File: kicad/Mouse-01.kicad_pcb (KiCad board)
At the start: 2 copper layers, 54 x 62 mm, 92 parts, among them P1 MT-ENC, P2 MT-ENC, P3 Battery_A, P4 Battery_B, P5 SWD, P6 UART, Q1 IRLML6402, Q2 IRFML8244, Q3 IRFML8244, Q4 BSS138, SW1 RESET, SW2 Power, SW3 BUTTON, U1 STM32F405RGTx, U2 DRV8835, U3 DRV8835, U4 LXDC55FAAA-203, U5 REF1933, U6 LT1963ES8, U7 AD8604, U8 MPU6500

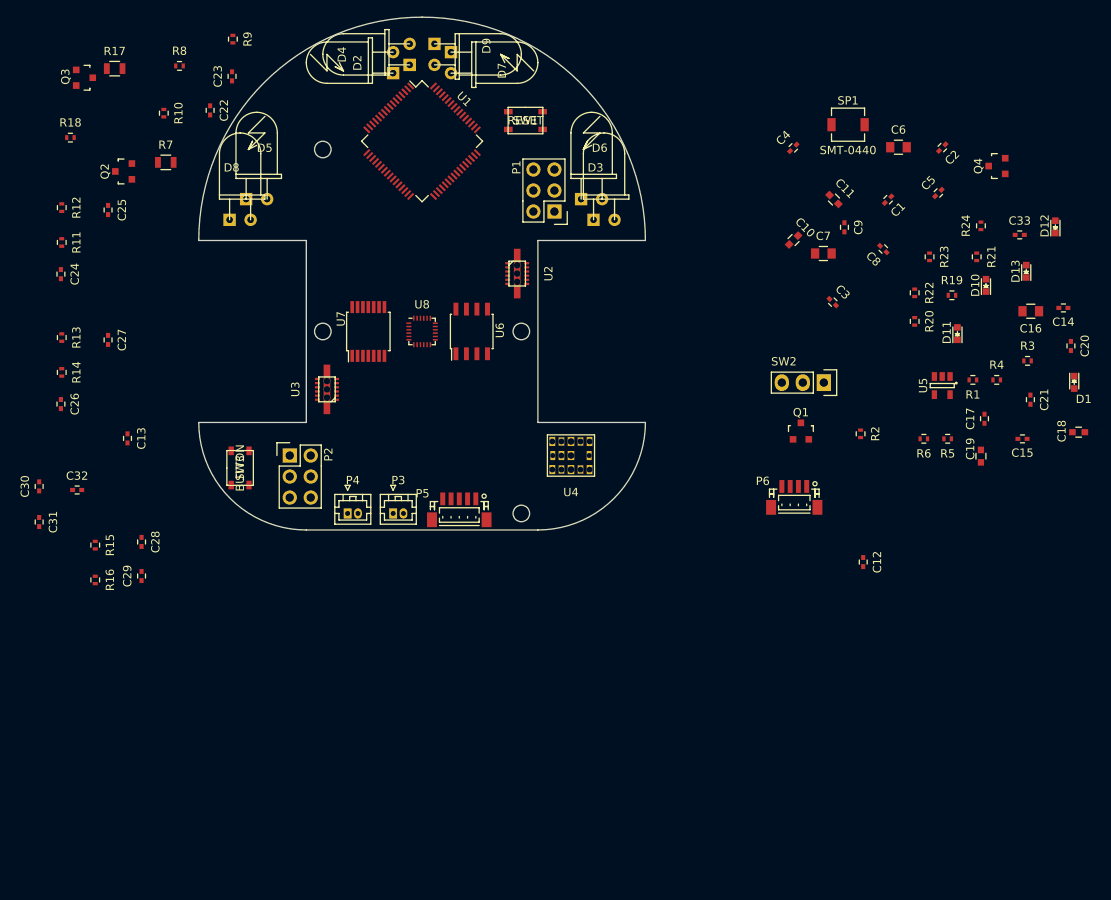
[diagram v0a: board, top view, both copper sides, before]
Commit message: 大きめの部品を配置
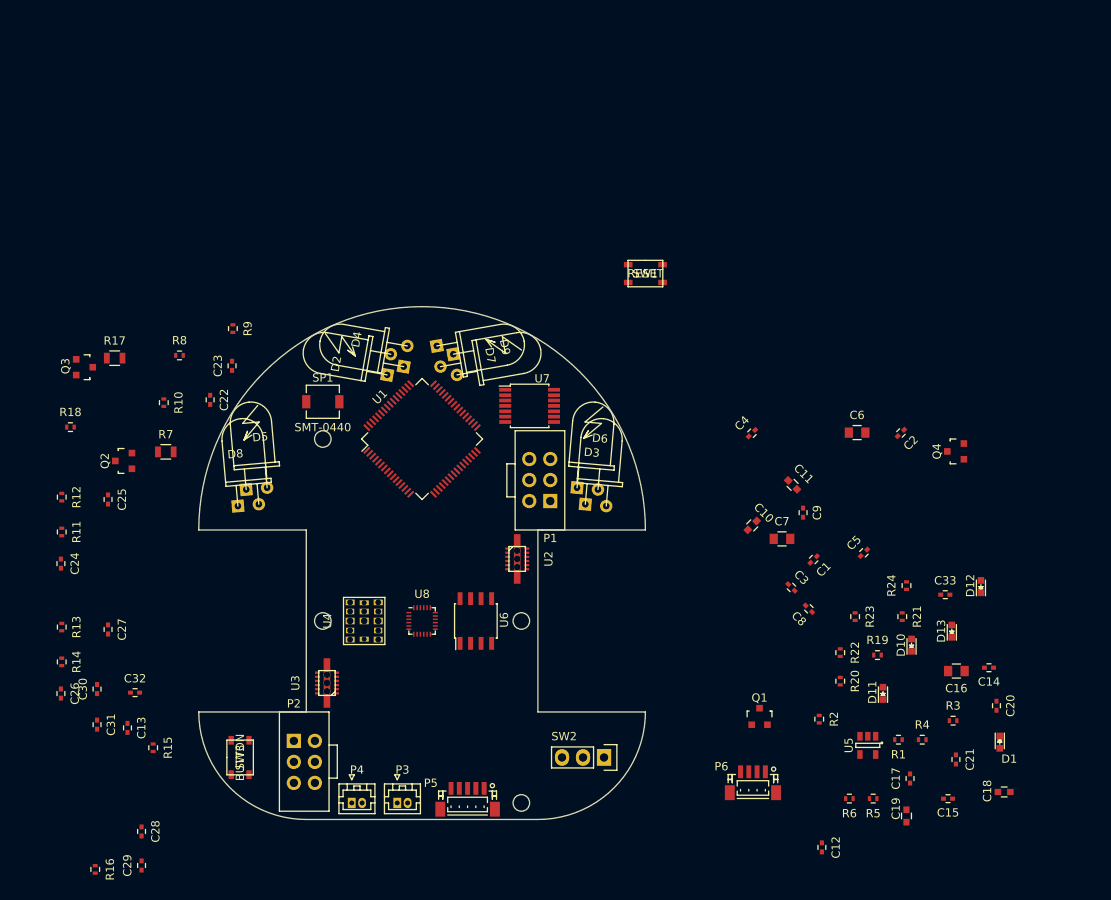
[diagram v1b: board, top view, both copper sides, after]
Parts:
- P1, P2: footprint Pin_Headers:Pin_Header_Straight_2x03 -> mouse:1717
- moved SP1 71.8 mm to (131.0, 107.5)
- moved SW2 52.5 mm to (165.0, 150.5)
- moved C15 44.4 mm to (206.6, 155.5)
- moved C18 44.4 mm to (213.4, 154.7)
- moved C20 44.4 mm to (212.4, 144.2)
- moved C21 44.4 mm to (207.5, 150.7)
- moved C8 44.4 mm to (189.8, 132.5)
- moved D13 44.4 mm to (207.0, 135.2)
- moved R21 44.4 mm to (201.1, 133.5)
- moved R23 44.4 mm to (195.4, 133.5)
- moved R24 44.4 mm to (201.6, 129.7)
- moved C1 44.4 mm to (190.3, 126.6)
- moved C14 44.4 mm to (211.5, 139.7)
- moved C16 44.4 mm to (207.6, 140.1)
- moved C17 44.4 mm to (202.0, 153.0)
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
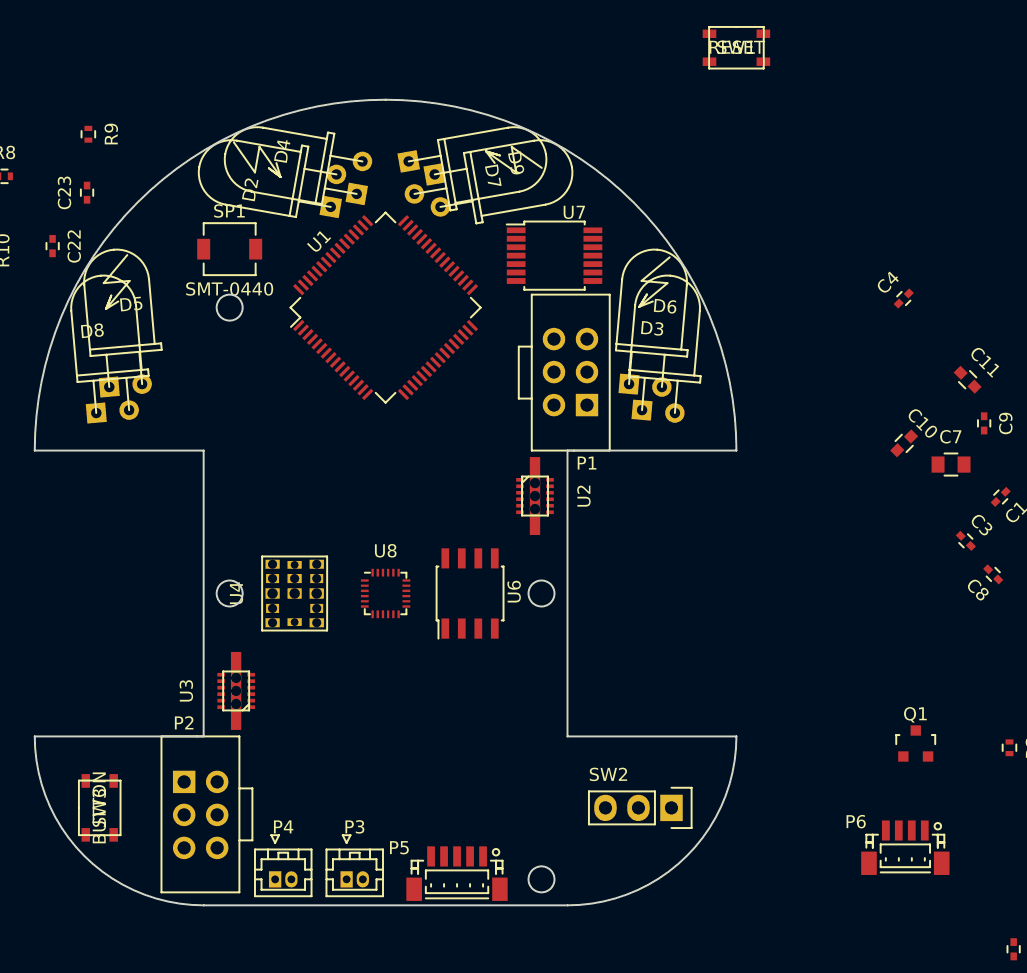
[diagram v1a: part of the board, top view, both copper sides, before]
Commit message: フットプリント調整
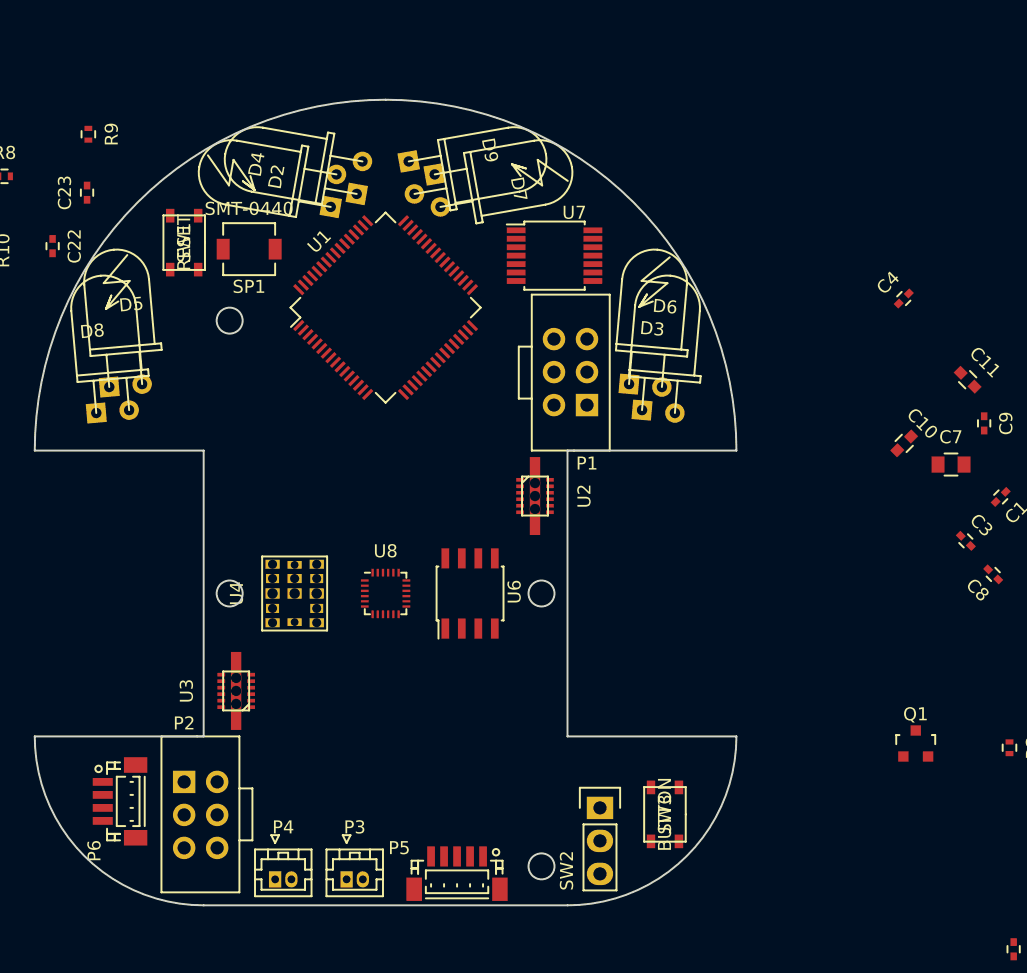
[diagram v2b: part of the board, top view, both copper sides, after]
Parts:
- moved P6 60.6 mm to (122.5, 150.0), turned to 270 degrees
- moved SW1 45.1 mm to (127.5, 107.0), turned to 270 degrees
- moved SW3 43.5 mm to (164.5, 151.0), turned to 270 degrees
- moved SW2 5.50 mm to (159.5, 150.5), turned to 0 degrees
- moved D2 2.24 mm to (141.0, 102.0)
- moved D4 2.24 mm to (139.0, 103.0)
- moved D7 2.24 mm to (147.0, 103.0)
- moved D9 2.24 mm to (145.0, 102.0)
- moved SP1 1.50 mm to (132.5, 107.5), turned to 180 degrees
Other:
- outline, holes or cut-outs redrawn
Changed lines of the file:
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@@
     (links 0)
     (no_connects 234)
-    (area 96.51 90.124999 215.239191 166.700001)
+    (area 96.51 95.899999 215.239191 166.700001)
     (thickness 1)
     (drawings 57)
@@
   )
   (module Pin_Headers:Pin_Header_Straight_1x03 placed (layer F.Cu)
-    (at 165 150.5 270)
+    (at 159.5 150.5)
     (descr "Through hole pin header")
     (tags "pin header")
-    (fp_text reference SW2 (at -2.54 4.826 360) (layer F.SilkS)
+    (fp_text reference SW2 (at -2.54 4.826 90) (layer F.SilkS)
       (effects (font (size 1 1) (thickness 0.15)))
     )
-    (fp_text value Power (at 0 -2.413 270) (layer F.Fab)
+    (fp_text value Power (at 0 -2.413) (layer F.Fab)
       (effects (font (size 1 1) (thickness 0.15)))
     )
@@
     (fp_line (start -1.55 0) (end -1.55 -1.55) (layer F.SilkS) (width 0.15))
     (fp_line (start -1.55 -1.55) (end 1.55 -1.55) (layer F.SilkS) (width 0.15))
-    (pad 1 thru_hole rect (at 0 0 270) (size 2.032 1.7272) (drill 1.016) (layers *.Cu *.Mask F.SilkS))
-    (pad 2 thru_hole oval (at 0 2.54 270) (size 2.032 1.7272) (drill 1.016) (layers *.Cu *.Mask F.SilkS)
+    (pad 1 thru_hole rect (at 0 0) (size 2.032 1.7272) (drill 1.016) (layers *.Cu *.Mask F.SilkS))
+    (pad 2 thru_hole oval (at 0 2.54) (size 2.032 1.7272) (drill 1.016) (layers *.Cu *.Mask F.SilkS)
       (net 36 "Net-(Q1-Pad1)"))
-    (pad 3 thru_hole oval (at 0 5.08 270) (size 2.032 1.7272) (drill 1.016) (layers *.Cu *.Mask F.SilkS)
+    (pad 3 thru_hole oval (at 0 5.08) (size 2.032 1.7272) (drill 1.016) (layers *.Cu *.Mask F.SilkS)
       (net 2 GND))
     (model Pin_Headers.3dshapes/Pin_Header_Straight_1x03.wrl
@@
   )
   (module Connectors_JST:JST_SH_BM04B-SRSS-TB_04x1.00mm_Straight (layer F.Cu)
-    (at 183 153.5 180)
+    (at 122.5 150 270)
     (descr http://www.jst-mfg.com/product/pdf/eng/eSH.pdf)
     (tags "connector jst sh")
     (attr smd)
-    (fp_text reference P6 (at 3.81 1.905 180) (layer F.SilkS)
+    (fp_text reference P6 (at 3.81 1.905 270) (layer F.SilkS)
       (effects (font (size 1 1) (thickness 0.15)))
     )
-    (fp_text value UART (at 0 3.5 180) (layer F.Fab)
+    (fp_text value UART (at 2 3.5 270) (layer F.Fab)
       (effects (font (size 1 1) (thickness 0.15)))
     )
@@
     (fp_line (start 3.9 -2.7) (end 3.9 2.55) (layer F.CrtYd) (width 0.05))
     (fp_line (start 3.9 2.55) (end -3.9 2.55) (layer F.CrtYd) (width 0.05))
-    (pad 1 smd rect (at -1.5 1.2625 180) (size 0.6 1.55) (layers F.Cu F.Paste F.Mask)
+    (pad 1 smd rect (at -1.5 1.2625 270) (size 0.6 1.55) (layers F.Cu F.Paste F.Mask)
       (net 1 +3V3))
-    (pad 2 smd rect (at -0.5 1.2625 180) (size 0.6 1.55) (layers F.Cu F.Paste F.Mask)
+    (pad 2 smd rect (at -0.5 1.2625 270) (size 0.6 1.55) (layers F.Cu F.Paste F.Mask)
       (net 2 GND))
-    (pad 3 smd rect (at 0.5 1.2625 180) (size 0.6 1.55) (layers F.Cu F.Paste F.Mask)
+    (pad 3 smd rect (at 0.5 1.2625 270) (size 0.6 1.55) (layers F.Cu F.Paste F.Mask)
       (net 34 UART-RX))
-    (pad 4 smd rect (at 1.5 1.2625 180) (size 0.6 1.55) (layers F.Cu F.Paste F.Mask)
+    (pad 4 smd rect (at 1.5 1.2625 270) (size 0.6 1.55) (layers F.Cu F.Paste F.Mask)
       (net 35 UART-TX))
-    (pad "" smd rect (at -2.8 -1.2625 180) (size 1.2 1.8) (layers F.Cu F.Paste F.Mask))
-    (pad "" smd rect (at 2.8 -1.2625 180) (size 1.2 1.8) (layers F.Cu F.Paste F.Mask))
+    (pad "" smd rect (at -2.8 -1.2625 270) (size 1.2 1.8) (layers F.Cu F.Paste F.Mask))
+    (pad "" smd rect (at 2.8 -1.2625 270) (size 1.2 1.8) (layers F.Cu F.Paste F.Mask))
   )
   (module Capacitors_SMD:C_0402 (layer F.Cu)
@@
   )
   (module mouse:SMT-0440-S-R (layer F.Cu)
-    (at 131 107.5)
-    (fp_text reference SP1 (at 0 -2.9) (layer F.SilkS)
+    (at 132.5 107.5 180)
+    (fp_text reference SP1 (at 0 -2.9 180) (layer F.SilkS)
       (effects (font (size 1 1) (thickness 0.15)))
     )
-    (fp_text value SMT-0440 (at 0 3.1) (layer F.SilkS)
+    (fp_text value SMT-0440 (at 0 3.1 180) (layer F.SilkS)
       (effects (font (size 1 1) (thickness 0.15)))
     )
@@
     (fp_line (start 2 -2) (end 2 -1.1) (layer F.SilkS) (width 0.15))
     (fp_line (start -2 -1.1) (end -2 -2) (layer F.SilkS) (width 0.15))
-    (pad 1 smd rect (at -2 0) (size 1 1.6) (layers F.Cu F.Paste F.Mask)
+    (pad 1 smd rect (at -2 0 180) (size 1 1.6) (layers F.Cu F.Paste F.Mask)
       (net 1 +3V3))
-    (pad 2 smd rect (at 2 0) (size 1 1.6) (layers F.Cu F.Paste F.Mask)
+    (pad 2 smd rect (at 2 0 180) (size 1 1.6) (layers F.Cu F.Paste F.Mask)
       (net 68 "Net-(Q4-Pad3)"))
   )
@@
   )
   (module mouse:LED-5MM_Angle placed (layer F.Cu)
-    (at 139 103 80)
+    (at 141 102 80)
     (descr "LED 5mm round vertical")
     (tags "LED 5mm round vertical")
@@
   )
   (module mouse:Photo-5MM_Angle placed (layer F.Cu)
-    (at 145 102 280)
+    (at 147 103 280)
     (descr "LED 5mm round vertical")
     (tags "LED 5mm round vertical")
@@
   )
   (module mouse:LED-5MM_Angle placed (layer F.Cu)
-    (at 147 103 280)
+    (at 145 102 280)
     (descr "LED 5mm round vertical")
     (tags "LED 5mm round vertical")
@@
   )
   (module mouse:Photo-5MM_Angle placed (layer F.Cu)
-    (at 141 102 80)
+    (at 139 103 80)
     (descr "LED 5mm round vertical")
     (tags "LED 5mm round vertical")
@@
   )
   (module mouse:SW_PUSH (layer F.Cu)
-    (at 170 92)
-    (fp_text reference SW1 (at 0 0) (layer F.SilkS)
+    (at 127.5 107 270)
+    (fp_text reference SW1 (at 0 0 270) (layer F.SilkS)
       (effects (font (size 1 1) (thickness 0.15)))
     )
-    (fp_text value RESET (at 0 0) (layer F.SilkS)
+    (fp_text value RESET (at 0 0 270) (layer F.SilkS)
       (effects (font (size 1 1) (thickness 0.15)))
     )
@@
     (fp_line (start 2.1 1.6) (end 2.1 -1.6) (layer F.SilkS) (width 0.15))
     (fp_line (start 2.1 -1.6) (end 0 -1.6) (layer F.SilkS) (width 0.15))
-    (pad 4 smd rect (at 2.075 1.075) (size 1.05 0.65) (layers F.Cu F.Paste F.Mask)
+    (pad 4 smd rect (at 2.075 1.075 270) (size 1.05 0.65) (layers F.Cu F.Paste F.Mask)
       (net 2 GND))
-    (pad 3 smd rect (at -2.075 1.075) (size 1.05 0.65) (layers F.Cu F.Paste F.Mask))
-    (pad 1 smd rect (at -2.075 -1.075) (size 1.05 0.65) (layers F.Cu F.Paste F.Mask))
-    (pad 2 smd rect (at 2.075 -1.075) (size 1.05 0.65) (layers F.Cu F.Paste F.Mask)
+    (pad 3 smd rect (at -2.075 1.075 270) (size 1.05 0.65) (layers F.Cu F.Paste F.Mask))
+    (pad 1 smd rect (at -2.075 -1.075 270) (size 1.05 0.65) (layers F.Cu F.Paste F.Mask))
+    (pad 2 smd rect (at 2.075 -1.075 270) (size 1.05 0.65) (layers F.Cu F.Paste F.Mask)
       (net 3 RESET))
   )
   (module mouse:SW_PUSH (layer F.Cu)
-    (at 121 150.5 90)
-    (fp_text reference SW3 (at 0 0 90) (layer F.SilkS)
+    (at 164.5 151 270)
+    (fp_text reference SW3 (at 0 0 270) (layer F.SilkS)
       (effects (font (size 1 1) (thickness 0.15)))
     )
-    (fp_text value BUTTON (at 0 0 90) (layer F.SilkS)
+    (fp_text value BUTTON (at 0 0 270) (layer F.SilkS)
       (effects (font (size 1 1) (thickness 0.15)))
     )
@@
     (fp_line (start 2.1 1.6) (end 2.1 -1.6) (layer F.SilkS) (width 0.15))
     (fp_line (start 2.1 -1.6) (end 0 -1.6) (layer F.SilkS) (width 0.15))
-    (pad 4 smd rect (at 2.075 1.075 90) (size 1.05 0.65) (layers F.Cu F.Paste F.Mask)
+    (pad 4 smd rect (at 2.075 1.075 270) (size 1.05 0.65) (layers F.Cu F.Paste F.Mask)
       (net 2 GND))
-    (pad 3 smd rect (at -2.075 1.075 90) (size 1.05 0.65) (layers F.Cu F.Paste F.Mask))
-    (pad 1 smd rect (at -2.075 -1.075 90) (size 1.05 0.65) (layers F.Cu F.Paste F.Mask))
-    (pad 2 smd rect (at 2.075 -1.075 90) (size 1.05 0.65) (layers F.Cu F.Paste F.Mask)
+    (pad 3 smd rect (at -2.075 1.075 270) (size 1.05 0.65) (layers F.Cu F.Paste F.Mask))
+    (pad 1 smd rect (at -2.075 -1.075 270) (size 1.05 0.65) (layers F.Cu F.Paste F.Mask))
+    (pad 2 smd rect (at 2.075 -1.075 270) (size 1.05 0.65) (layers F.Cu F.Paste F.Mask)
       (net 18 BUTTON))
   )
@@
   (gr_line (start 170 134) (end 143 134) (angle 90) (layer Eco1.User) (width 0.2))
   (gr_line (start 116 134) (end 170 134) (angle 90) (layer Eco1.User) (width 0.2))
-  (gr_circle (center 155 156) (end 156 156) (layer Edge.Cuts) (width 0.15))
+  (gr_circle (center 155 155) (end 156 155) (layer Edge.Cuts) (width 0.15))
   (gr_circle (center 155 134) (end 156 134) (layer Edge.Cuts) (width 0.15))
   (gr_line (start 124 144) (end 125 144) (angle 90) (layer Eco1.User) (width 0.2))
-  (gr_circle (center 131 112) (end 132 112) (layer Edge.Cuts) (width 0.15))
+  (gr_circle (center 131 113) (end 132 113) (layer Edge.Cuts) (width 0.15))
   (gr_circle (center 131 134) (end 132 134) (layer Edge.Cuts) (width 0.15))
   (gr_line (start 129 145) (end 116 145) (angle 90) (layer Edge.Cuts) (width 0.15))

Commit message: 徐々に部品を配置，部品の確認
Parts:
- removed the C6 at (195.6, 111.2)
- removed the C7 at (186.5, 124.1)
- removed the R4 at (203.5, 148.4)
- added C12: 22u, Capacitors_SMD:C_0805, F.Cu at (149.0, 129.5)
- R2: value 1k -> 10k
- R5: renamed from R6; value 68 -> 133
- moved C14 82.9 mm to (157.0, 89.0)
- moved C17 77.1 mm to (153.0, 106.8)
- moved C20 75.6 mm to (160.0, 92.0)
- moved C16 68.4 mm to (153.0, 105.2), turned to 180 degrees
- moved C19 68.4 mm to (166.0, 94.0)
- moved C10 67.9 mm to (167.0, 98.0)
- moved C18 66.2 mm to (160.0, 106.0)
- moved C2 64.3 mm to (140.0, 90.5)
- moved C7 63.5 mm to (126.5, 110.0), turned to 180 degrees
- moved C13 59.5 mm to (152.0, 138.8), turned to 270 degrees
- moved U5 58.8 mm to (156.8, 106.0), turned to 180 degrees
- moved C5 58.8 mm to (138.0, 119.5), turned to 135 degrees
- moved C15 58.6 mm to (149.0, 138.5), turned to 0 degrees
- moved C32 56.3 mm to (162.0, 96.0)
- moved C6 54.7 mm to (153.0, 92.0)
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- renumbered C12 to C10, C13 to C11, C14 to C13, C15 to C14, C16 to C15, C17 to C16, C18 to C17, C19 to C18, C20 to C19, C21 to C20, C22 to C21, C23 to C22, C24 to C23, C25 to C24, C26 to C25, C27 to C26, C28 to C27, C29 to C28, C30 to C29, C31 to C30, C32 to C31, C33 to C32, C8 to C6, C9 to C7, C10 to C8, C11 to C9, R11 to R10, R12 to R11, R13 to R12, R14 to R13, R15 to R14, R16 to R15, R17 to R16, R18 to R17, R19 to R18, R20 to R19, R21 to R20, R22 to R21, R23 to R22, R24 to R23, R5 to R4, R7 to R6, R8 to R7, R9 to R8, R10 to R9
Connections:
- R5 pad 1: Net-(R4-Pad1) -> Net-(R5-Pad1)
- U1 pad 16: MT-IN-R-1 -> UART-TX
- U1 pad 17: MT-IN-R-2 -> UART-RX
- U1 pad 29: (no net) -> MT-IN-R-1
- U1 pad 30: (no net) -> MT-IN-R-2
- U1 pad 42: UART-TX -> (no net)
- U1 pad 43: UART-RX -> (no net)
- U1 pad 61: (no net) -> SPEAKER
- U1 pad 62: SPEAKER -> (no net)
- U4 pad 11: Net-(R4-Pad2) -> Net-(R5-Pad1)

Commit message: とりあえず全部品を配置
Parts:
- removed the R18 at (198.1, 138.1)
- SW2: footprint Pin_Headers:Pin_Header_Straight_1x03 -> mouse:Slide_SW
- moved Q4 94.0 mm to (120.2, 148.5)
- moved D1 83.9 mm to (143.0, 102.2), turned to 90 degrees
- moved R22 80.3 mm to (123.5, 148.5)
- moved D10 76.5 mm to (136.0, 98.5), turned to 270 degrees
- moved R3 74.4 mm to (133.0, 151.0), turned to 90 degrees
- moved D11 73.4 mm to (140.5, 98.0), turned to 270 degrees
- moved R15 73.1 mm to (148.0, 106.0), turned to 0 degrees
- moved D12 72.4 mm to (145.5, 98.0), turned to 270 degrees
- moved R18 70.5 mm to (137.5, 98.5), turned to 90 degrees
- moved R19 68.9 mm to (142.0, 98.0), turned to 90 degrees
- moved D13 67.8 mm to (150.0, 98.5), turned to 270 degrees
- moved R2 66.4 mm to (143.0, 100.0), turned to 0 degrees
- moved R13 65.1 mm to (162.2, 122.0), turned to 0 degrees
- moved C14 63.7 mm to (152.0, 152.5), turned to 270 degrees
- moved R20 63.6 mm to (144.0, 98.0), turned to 90 degrees
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- renumbered R19 to R18, R20 to R19, R21 to R20, R22 to R21, R23 to R22
